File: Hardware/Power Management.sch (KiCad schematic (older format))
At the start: 15 parts

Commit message: Motor driver and power management subsheet converted to blocks
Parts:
- removed TP?: Bat+, TestPoint:TestPoint_Keystone_5000-5004_Miniature, symbol Connector:TestPoint
- removed TP?: Bat-, TestPoint:TestPoint_Keystone_5000-5004_Miniature, symbol Connector:TestPoint
- removed TP?: TestPoint_2Pole, TestPoint:TestPoint_2Pads_Pitch2.54mm_Drill0.8mm, symbol Connector:TestPoint_2Pole
- added C?: 220nF, Capacitor_Tantalum_SMD:CP_EIA-3216-18_Kemet-A, symbol Device:CP_Small
- added C? (x2): 4.7uF, Capacitor_Tantalum_SMD:CP_EIA-3528-15_AVX-H, symbol Device:CP_Small
- added C?: 100nF, Capacitor_SMD:C_0805_2012Metric, symbol Device:C_Small
- added C?: 100uF, Capacitor_Tantalum_SMD:CP_EIA-7343-31_Kemet-D, symbol Device:CP_Small
- added D?: GREEN, symbol Device:LED_Small
- added D?: 5A, Diode_SMD:D_SOD-123F, symbol Device:D_Schottky
- added L?: 15uH, Inductor_SMD:L_Neosid_SMs42, symbol Device:L_Small
- added R?: 10K, Resistor_SMD:R_0805_2012Metric, symbol Device:R_Small_US
- added R?: 5.8k, Resistor_SMD:R_0805_2012Metric, symbol Device:R_Small_US
- added R?: 4.7k, Resistor_SMD:R_0805_2012Metric, symbol Device:R_Small_US
- added U?: TPS56628, Package_SO:HSOP-8-1EP_3.9x4.9mm_P1.27mm_EP2.41x3.1mm_ThermalVias, symbol Power_Management:TPS56628
- gave numbers to parts that had none: 12
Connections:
- net labels added: 3.3V, 9V, SNS3, SNS9, VBAT
- net labels removed: +3.3V, VSNS3
- wire segments 44 -> 86
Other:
- moved on the sheet: C4, C5, C6, C7, C8, D1, D2, L1, R5, R6, R7

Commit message: Readme updated
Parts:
- gave numbers to parts that had none: 12
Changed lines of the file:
@@
 P 4150 3350
 AR Path="/5FF19FDD" Ref="#PWR?"  Part="1"
-AR Path="/5FF0069C/5FF19FDD" Ref="#PWR012"  Part="1"
-F 0 "#PWR012" H 4150 3200 50  0001 C CNN
+AR Path="/5FF0069C/5FF19FDD" Ref="#PWR015"  Part="1"
+F 0 "#PWR015" H 4150 3200 50  0001 C CNN
 F 1 "+BATT" H 4165 3523 50  0000 C CNN
 F 2 "" H 4150 3350 50  0001 C CNN
@@
 P 5600 3950
 AR Path="/5FF1A004" Ref="#PWR?"  Part="1"
-AR Path="/5FF0069C/5FF1A004" Ref="#PWR014"  Part="1"
-F 0 "#PWR014" H 5600 3700 50  0001 C CNN
+AR Path="/5FF0069C/5FF1A004" Ref="#PWR016"  Part="1"
+F 0 "#PWR016" H 5600 3700 50  0001 C CNN
 F 1 "GND" H 5605 3777 50  0000 C CNN
 F 2 "" H 5600 3950 50  0001 C CNN
@@
 AR Path="/5E9DAA7B/5FF43866" Ref="C?"  Part="1"
 AR Path="/5FF43866" Ref="C?"  Part="1"
-AR Path="/5FF0069C/5FF43866" Ref="C?"  Part="1"
-F 0 "C?" H 4638 5096 50  0000 L CNN
+AR Path="/5FF0069C/5FF43866" Ref="C11"  Part="1"
+F 0 "C11" H 4638 5096 50  0000 L CNN
 F 1 "220nF" H 4638 5005 50  0000 L CNN
 F 2 "Capacitor_Tantalum_SMD:CP_EIA-3216-18_Kemet-A" H 4550 5050 50  0001 C CNN
@@
 AR Path="/5E9DAA7B/5FF4386C" Ref="C?"  Part="1"
 AR Path="/5FF4386C" Ref="C?"  Part="1"
-AR Path="/5FF0069C/5FF4386C" Ref="C?"  Part="1"
-F 0 "C?" H 4238 5096 50  0000 L CNN
+AR Path="/5FF0069C/5FF4386C" Ref="C10"  Part="1"
+F 0 "C10" H 4238 5096 50  0000 L CNN
 F 1 "4.7uF" H 4238 5005 50  0000 L CNN
 F 2 "Capacitor_Tantalum_SMD:CP_EIA-3528-15_AVX-H" H 4150 5050 50  0001 C CNN
@@
 AR Path="/5E9DAA7B/5FF43873" Ref="L?"  Part="1"
 AR Path="/5FF43873" Ref="L?"  Part="1"
-AR Path="/5FF0069C/5FF43873" Ref="L?"  Part="1"
-F 0 "L?" V 6835 4800 50  0000 C CNN
+AR Path="/5FF0069C/5FF43873" Ref="L2"  Part="1"
+F 0 "L2" V 6835 4800 50  0000 C CNN
 F 1 "15uH" V 6744 4800 50  0000 C CNN
 F 2 "Inductor_SMD:L_Neosid_SMs42" H 6650 4800 50  0001 C CNN
@@
 AR Path="/5E9DAA7B/5FF43879" Ref="C?"  Part="1"
 AR Path="/5FF43879" Ref="C?"  Part="1"
-AR Path="/5FF0069C/5FF43879" Ref="C?"  Part="1"
-F 0 "C?" V 5971 4800 50  0000 C CNN
+AR Path="/5FF0069C/5FF43879" Ref="C9"  Part="1"
+F 0 "C9" V 5971 4800 50  0000 C CNN
 F 1 "100nF" V 6062 4800 50  0000 C CNN
 F 2 "Capacitor_SMD:C_0805_2012Metric" H 6200 4800 50  0001 C CNN
@@
 P 4150 4750
 AR Path="/5FF43888" Ref="#PWR?"  Part="1"
-AR Path="/5FF0069C/5FF43888" Ref="#PWR?"  Part="1"
-F 0 "#PWR?" H 4150 4600 50  0001 C CNN
+AR Path="/5FF0069C/5FF43888" Ref="#PWR017"  Part="1"
+F 0 "#PWR017" H 4150 4600 50  0001 C CNN
 F 1 "+BATT" H 4165 4923 50  0000 C CNN
 F 2 "" H 4150 4750 50  0001 C CNN
@@
 AR Path="/5E9DAA7B/5FF43896" Ref="R?"  Part="1"
 AR Path="/5FF43896" Ref="R?"  Part="1"
-AR Path="/5FF0069C/5FF43896" Ref="R?"  Part="1"
-F 0 "R?" H 7718 4900 50  0000 L BNN
+AR Path="/5FF0069C/5FF43896" Ref="R8"  Part="1"
+F 0 "R8" H 7718 4900 50  0000 L BNN
 F 1 "10K" H 7718 4855 50  0000 L CNN
 F 2 "Resistor_SMD:R_0805_2012Metric" H 7650 4900 50  0001 C CNN
@@
 AR Path="/5E9DAA7B/5FF4389C" Ref="R?"  Part="1"
 AR Path="/5FF4389C" Ref="R?"  Part="1"
-AR Path="/5FF0069C/5FF4389C" Ref="R?"  Part="1"
-F 0 "R?" H 7718 5200 50  0000 L BNN
+AR Path="/5FF0069C/5FF4389C" Ref="R10"  Part="1"
+F 0 "R10" H 7718 5200 50  0000 L BNN
 F 1 "5.8k" H 7718 5155 50  0000 L CNN
 F 2 "Resistor_SMD:R_0805_2012Metric" H 7650 5200 50  0001 C CNN
@@
 P 5600 5350
 AR Path="/5FF438A6" Ref="#PWR?"  Part="1"
-AR Path="/5FF0069C/5FF438A6" Ref="#PWR?"  Part="1"
-F 0 "#PWR?" H 5600 5100 50  0001 C CNN
+AR Path="/5FF0069C/5FF438A6" Ref="#PWR018"  Part="1"
+F 0 "#PWR018" H 5600 5100 50  0001 C CNN
 F 1 "GND" H 5605 5177 50  0000 C CNN
 F 2 "" H 5600 5350 50  0001 C CNN
@@
 P 4550 4750
 AR Path="/5FF438AD" Ref="#FLG?"  Part="1"
-AR Path="/5FF0069C/5FF438AD" Ref="#FLG?"  Part="1"
-F 0 "#FLG?" H 4550 4825 50  0001 C CNN
+AR Path="/5FF0069C/5FF438AD" Ref="#FLG04"  Part="1"
+F 0 "#FLG04" H 4550 4825 50  0001 C CNN
 F 1 "PWR_FLAG" H 4550 4923 50  0000 C CNN
 F 2 "" H 4550 4750 50  0001 C CNN
@@
 P 4550 5350
 AR Path="/5FF438B4" Ref="#FLG?"  Part="1"
-AR Path="/5FF0069C/5FF438B4" Ref="#FLG?"  Part="1"
-F 0 "#FLG?" H 4550 5425 50  0001 C CNN
+AR Path="/5FF0069C/5FF438B4" Ref="#FLG06"  Part="1"
+F 0 "#FLG06" H 4550 5425 50  0001 C CNN
 F 1 "PWR_FLAG" H 4550 5523 50  0000 C CNN
 F 2 "" H 4550 5350 50  0001 C CNN
@@
 P 7250 4750
 AR Path="/5FF438BB" Ref="#FLG?"  Part="1"
-AR Path="/5FF0069C/5FF438BB" Ref="#FLG?"  Part="1"
-F 0 "#FLG?" H 7250 4825 50  0001 C CNN
+AR Path="/5FF0069C/5FF438BB" Ref="#FLG05"  Part="1"
+F 0 "#FLG05" H 7250 4825 50  0001 C CNN
 F 1 "PWR_FLAG" H 7250 4923 50  0000 C CNN
 F 2 "" H 7250 4750 50  0001 C CNN
@@
 P 5600 4700
 AR Path="/5FF438C6" Ref="U?"  Part="1"
-AR Path="/5FF0069C/5FF438C6" Ref="U?"  Part="1"
-F 0 "U?" H 5600 4865 50  0000 C CNN
+AR Path="/5FF0069C/5FF438C6" Ref="U3"  Part="1"
+F 0 "U3" H 5600 4865 50  0000 C CNN
 F 1 "TPS56628" H 5600 4774 50  0000 C CNN
 F 2 "Package_SO:HSOP-8-1EP_3.9x4.9mm_P1.27mm_EP2.41x3.1mm_ThermalVias" H 5600 4850 50  0001 C CNN
@@
 P 5050 5100
 AR Path="/5FF438CF" Ref="D?"  Part="1"
-AR Path="/5FF0069C/5FF438CF" Ref="D?"  Part="1"
-F 0 "D?" H 4950 5200 50  0000 C CNN
+AR Path="/5FF0069C/5FF438CF" Ref="D4"  Part="1"
+F 0 "D4" H 4950 5200 50  0000 C CNN
 F 1 "GREEN" H 5150 5200 50  0000 C CNN
 F 2 "" V 5050 5100 50  0001 C CNN
@@
 AR Path="/5EA2026E/5FF438D5" Ref="R?"  Part="1"
 AR Path="/5FF438D5" Ref="R?"  Part="1"
-AR Path="/5FF0069C/5FF438D5" Ref="R?"  Part="1"
-F 0 "R?" V 5150 5050 50  0000 L CNN
+AR Path="/5FF0069C/5FF438D5" Ref="R9"  Part="1"
+F 0 "R9" V 5150 5050 50  0000 L CNN
 F 1 "4.7k" V 5100 4900 50  0000 L CNN
 F 2 "Resistor_SMD:R_0805_2012Metric" H 5050 5000 50  0001 C CNN
@@
 AR Path="/5E9DAA7B/5FF438EB" Ref="C?"  Part="1"
 AR Path="/5FF438EB" Ref="C?"  Part="1"
-AR Path="/5FF0069C/5FF438EB" Ref="C?"  Part="1"
-F 0 "C?" H 6938 5096 50  0000 L CNN
+AR Path="/5FF0069C/5FF438EB" Ref="C12"  Part="1"
+F 0 "C12" H 6938 5096 50  0000 L CNN
 F 1 "100uF" H 6938 5005 50  0000 L CNN
 F 2 "Capacitor_Tantalum_SMD:CP_EIA-7343-31_Kemet-D" H 6850 5050 50  0001 C CNN
@@
 AR Path="/5E9DAA7B/5FF438F1" Ref="C?"  Part="1"
 AR Path="/5FF438F1" Ref="C?"  Part="1"
-AR Path="/5FF0069C/5FF438F1" Ref="C?"  Part="1"
-F 0 "C?" H 7338 5096 50  0000 L CNN
+AR Path="/5FF0069C/5FF438F1" Ref="C13"  Part="1"
+F 0 "C13" H 7338 5096 50  0000 L CNN
 F 1 "4.7uF" H 7338 5005 50  0000 L CNN
 F 2 "Capacitor_Tantalum_SMD:CP_EIA-3528-15_AVX-H" H 7250 5050 50  0001 C CNN
@@
 AR Path="/5E9DAA7B/5FF438F7" Ref="D?"  Part="1"
 AR Path="/5FF438F7" Ref="D?"  Part="1"
-AR Path="/5FF0069C/5FF438F7" Ref="D?"  Part="1"
-F 0 "D?" V 6404 5129 50  0000 L CNN
+AR Path="/5FF0069C/5FF438F7" Ref="D3"  Part="1"
+F 0 "D3" V 6404 5129 50  0000 L CNN
 F 1 "5A" V 6495 5129 50  0000 L CNN
 F 2 "Diode_SMD:D_SOD-123F" V 6450 5050 50  0001 C CNN

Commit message: Tidying up
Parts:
- U2, U3: symbol Power_Management:TPS56628 -> tps56628:TPS56628
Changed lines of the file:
@@
 Tant
 $Comp
-L Power_Management:TPS56628 U?
+L tps56628:TPS56628 U?
 U 1 1 5FF1A031
 P 5600 3300
@@
 Tant
 $Comp
-L Power_Management:TPS56628 U?
+L tps56628:TPS56628 U?
 U 1 1 5FF438C6
 P 5600 4700

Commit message: Battery charger IC added
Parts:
- added TP? (x2): TestPoint, TestPoint:TestPoint_Loop_D1.80mm_Drill1.0mm_Beaded, symbol Connector:TestPoint
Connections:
- net 3.3V: now also TP?.1
- net 9V: now also TP?.1
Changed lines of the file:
@@
 Wire Wire Line
 	4150 4800 4100 4800
+$Comp
+L Connector:TestPoint TP?
+U 1 1 5FF08244
+P 7650 3350
+F 0 "TP?" H 7708 3422 50  0000 L CNN
+F 1 "TestPoint" H 7708 3377 50  0001 L CNN
+F 2 "TestPoint:TestPoint_Loop_D1.80mm_Drill1.0mm_Beaded" H 7850 3350 50  0001 C CNN
+F 3 "~" H 7850 3350 50  0001 C CNN
+	1    7650 3350
+	1    0    0    -1
+$EndComp
+Wire Wire Line
+	7650 3350 7650 3400
+$Comp
+L Connector:TestPoint TP?
+U 1 1 5FF0F95D
+P 7650 4750
+F 0 "TP?" H 7708 4822 50  0000 L CNN
+F 1 "TestPoint" H 7708 4777 50  0001 L CNN
+F 2 "TestPoint:TestPoint_Loop_D1.80mm_Drill1.0mm_Beaded" H 7850 4750 50  0001 C CNN
+F 3 "~" H 7850 4750 50  0001 C CNN
+	1    7650 4750
+	1    0    0    -1
+$EndComp
+Wire Wire Line
+	7650 4750 7650 4800
 $EndSCHEMATC

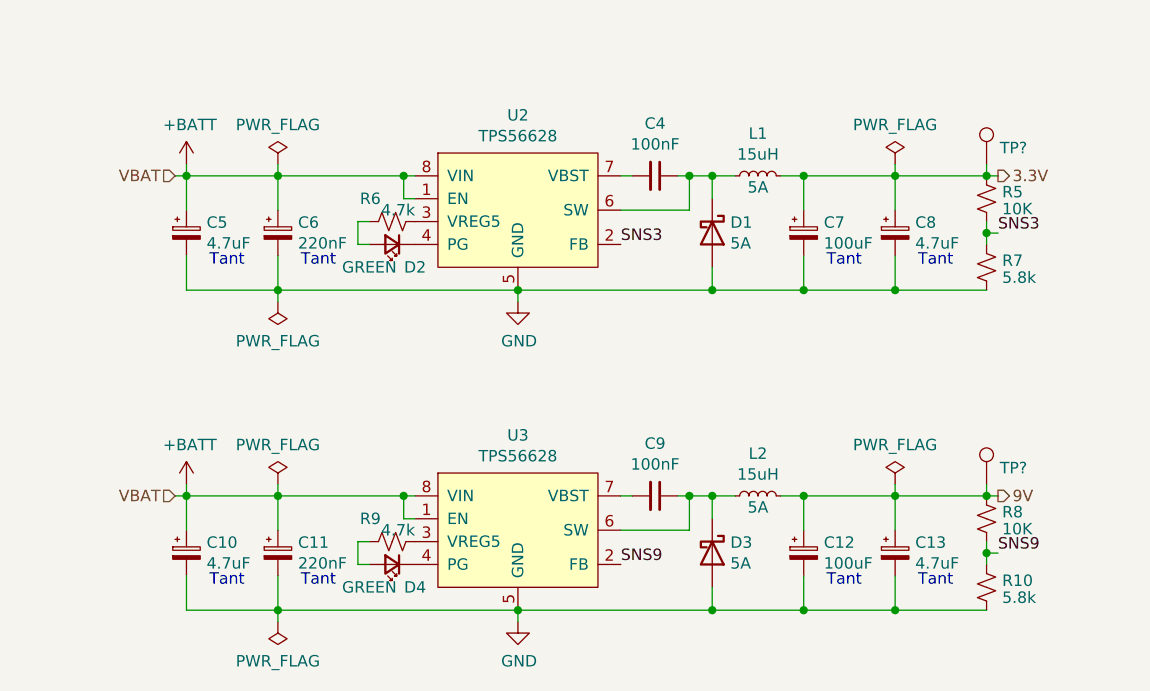
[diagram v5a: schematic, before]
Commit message: Replaced ESP-WROOM-32D with ESP32-CAM
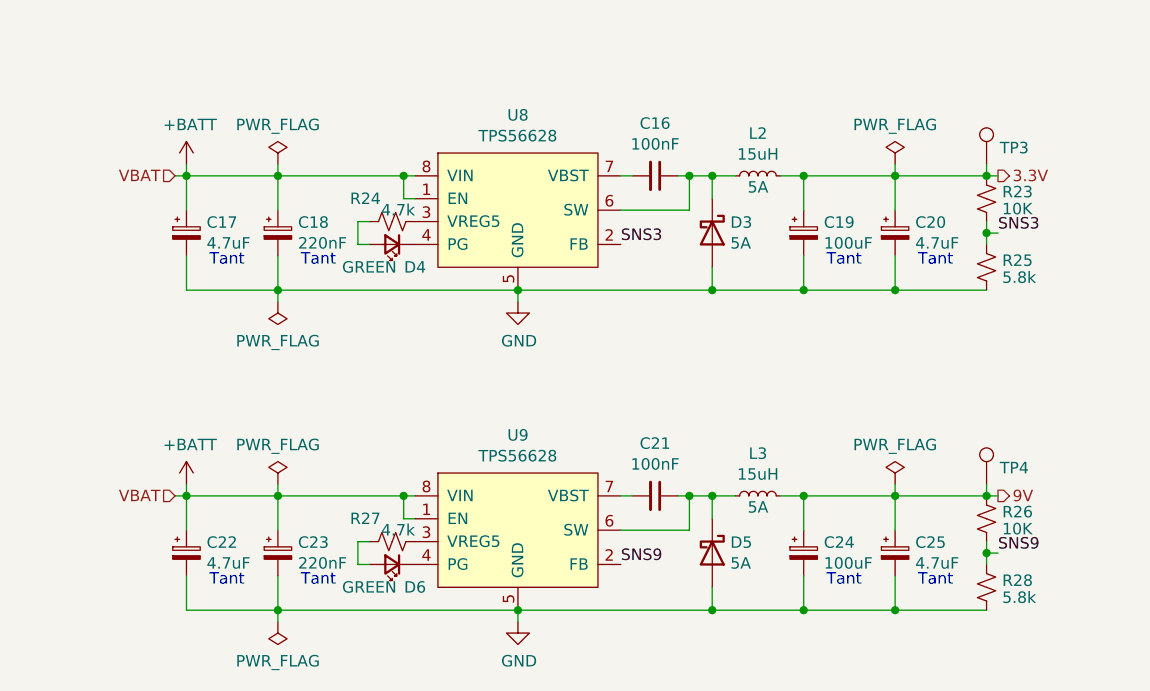
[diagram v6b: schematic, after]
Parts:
- gave numbers to parts that had none: 2
- renumbered C4 to C16, C5 to C17, C6 to C18, C7 to C19, C8 to C20, C9 to C21, C10 to C22, C11 to C23, C12 to C24, C13 to C25, D1 to D3, D2 to D4, D3 to D5, D4 to D6, L1 to L2, L2 to L3, R5 to R23, R6 to R24, R7 to R25, R8 to R26, R9 to R27, R10 to R28, U2 to U8, U3 to U9

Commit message: Signed-off-by: Usman <usmanmehmood55@gmail.com>
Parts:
- renumbered R23 to R25, R24 to R26, R25 to R27, R26 to R28, R27 to R29, R28 to R30
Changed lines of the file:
@@
 AR Path="/5E9DAA7B/5FF19FF3" Ref="R?"  Part="1"
 AR Path="/5FF19FF3" Ref="R?"  Part="1"
-AR Path="/5FF0069C/5FF19FF3" Ref="R23"  Part="1"
-F 0 "R23" H 7718 3500 50  0000 L BNN
+AR Path="/5FF0069C/5FF19FF3" Ref="R25"  Part="1"
+F 0 "R25" H 7718 3500 50  0000 L BNN
 F 1 "10K" H 7718 3455 50  0000 L CNN
 F 2 "Resistor_SMD:R_0805_2012Metric" H 7650 3500 50  0001 C CNN
@@
 AR Path="/5E9DAA7B/5FF19FF9" Ref="R?"  Part="1"
 AR Path="/5FF19FF9" Ref="R?"  Part="1"
-AR Path="/5FF0069C/5FF19FF9" Ref="R25"  Part="1"
-F 0 "R25" H 7718 3800 50  0000 L BNN
+AR Path="/5FF0069C/5FF19FF9" Ref="R27"  Part="1"
+F 0 "R27" H 7718 3800 50  0000 L BNN
 F 1 "5.8k" H 7718 3755 50  0000 L CNN
 F 2 "Resistor_SMD:R_0805_2012Metric" H 7650 3800 50  0001 C CNN
@@
 Wire Wire Line
 	5600 3950 5600 3900
-$Comp
-L power:PWR_FLAG #FLG?
-U 1 1 5FF1A018
-P 4550 3350
-AR Path="/5FF1A018" Ref="#FLG?"  Part="1"
-AR Path="/5FF0069C/5FF1A018" Ref="#FLG01"  Part="1"
-F 0 "#FLG01" H 4550 3425 50  0001 C CNN
-F 1 "PWR_FLAG" H 4550 3523 50  0000 C CNN
-F 2 "" H 4550 3350 50  0001 C CNN
-F 3 "~" H 4550 3350 50  0001 C CNN
-	1    4550 3350
-	1    0    0    -1
-$EndComp
-Wire Wire Line
-	4550 3350 4550 3400
-$Comp
-L power:PWR_FLAG #FLG?
-U 1 1 5FF1A01F
-P 4550 3950
-AR Path="/5FF1A01F" Ref="#FLG?"  Part="1"
-AR Path="/5FF0069C/5FF1A01F" Ref="#FLG03"  Part="1"
-F 0 "#FLG03" H 4550 4025 50  0001 C CNN
-F 1 "PWR_FLAG" H 4550 4123 50  0000 C CNN
-F 2 "" H 4550 3950 50  0001 C CNN
-F 3 "~" H 4550 3950 50  0001 C CNN
-	1    4550 3950
-	-1   0    0    1
-$EndComp
-Wire Wire Line
-	4550 3950 4550 3900
-$Comp
-L power:PWR_FLAG #FLG?
-U 1 1 5FF1A026
-P 7250 3350
-AR Path="/5FF1A026" Ref="#FLG?"  Part="1"
-AR Path="/5FF0069C/5FF1A026" Ref="#FLG02"  Part="1"
-F 0 "#FLG02" H 7250 3425 50  0001 C CNN
-F 1 "PWR_FLAG" H 7250 3523 50  0000 C CNN
-F 2 "" H 7250 3350 50  0001 C CNN
-F 3 "~" H 7250 3350 50  0001 C CNN
-	1    7250 3350
-	1    0    0    -1
-$EndComp
-Wire Wire Line
-	7250 3350 7250 3400
 Text Notes 6950 3800 0    50   ~ 0
 Tant
@@
 AR Path="/5EA2026E/5FF1A040" Ref="R?"  Part="1"
 AR Path="/5FF1A040" Ref="R?"  Part="1"
-AR Path="/5FF0069C/5FF1A040" Ref="R24"  Part="1"
-F 0 "R24" V 5150 3650 50  0000 L CNN
+AR Path="/5FF0069C/5FF1A040" Ref="R26"  Part="1"
+F 0 "R26" V 5150 3650 50  0000 L CNN
 F 1 "4.7k" V 5100 3500 50  0000 L CNN
 F 2 "Resistor_SMD:R_0805_2012Metric" H 5050 3600 50  0001 C CNN
@@
 AR Path="/5E9DAA7B/5FF43896" Ref="R?"  Part="1"
 AR Path="/5FF43896" Ref="R?"  Part="1"
-AR Path="/5FF0069C/5FF43896" Ref="R26"  Part="1"
-F 0 "R26" H 7718 4900 50  0000 L BNN
+AR Path="/5FF0069C/5FF43896" Ref="R28"  Part="1"
+F 0 "R28" H 7718 4900 50  0000 L BNN
 F 1 "10K" H 7718 4855 50  0000 L CNN
 F 2 "Resistor_SMD:R_0805_2012Metric" H 7650 4900 50  0001 C CNN
@@
 AR Path="/5E9DAA7B/5FF4389C" Ref="R?"  Part="1"
 AR Path="/5FF4389C" Ref="R?"  Part="1"
-AR Path="/5FF0069C/5FF4389C" Ref="R28"  Part="1"
-F 0 "R28" H 7718 5200 50  0000 L BNN
+AR Path="/5FF0069C/5FF4389C" Ref="R30"  Part="1"
+F 0 "R30" H 7718 5200 50  0000 L BNN
 F 1 "5.8k" H 7718 5155 50  0000 L CNN
 F 2 "Resistor_SMD:R_0805_2012Metric" H 7650 5200 50  0001 C CNN
@@
 Wire Wire Line
 	5600 5350 5600 5300
-$Comp
-L power:PWR_FLAG #FLG?
-U 1 1 5FF438AD
-P 4550 4750
-AR Path="/5FF438AD" Ref="#FLG?"  Part="1"
-AR Path="/5FF0069C/5FF438AD" Ref="#FLG04"  Part="1"
-F 0 "#FLG04" H 4550 4825 50  0001 C CNN
-F 1 "PWR_FLAG" H 4550 4923 50  0000 C CNN
-F 2 "" H 4550 4750 50  0001 C CNN
-F 3 "~" H 4550 4750 50  0001 C CNN
-	1    4550 4750
-	1    0    0    -1
-$EndComp
-Wire Wire Line
-	4550 4750 4550 4800
-$Comp
-L power:PWR_FLAG #FLG?
-U 1 1 5FF438B4
-P 4550 5350
-AR Path="/5FF438B4" Ref="#FLG?"  Part="1"
-AR Path="/5FF0069C/5FF438B4" Ref="#FLG06"  Part="1"
-F 0 "#FLG06" H 4550 5425 50  0001 C CNN
-F 1 "PWR_FLAG" H 4550 5523 50  0000 C CNN
-F 2 "" H 4550 5350 50  0001 C CNN
-F 3 "~" H 4550 5350 50  0001 C CNN
-	1    4550 5350
-	-1   0    0    1
-$EndComp
-Wire Wire Line
-	4550 5350 4550 5300
-$Comp
-L power:PWR_FLAG #FLG?
-U 1 1 5FF438BB
-P 7250 4750
-AR Path="/5FF438BB" Ref="#FLG?"  Part="1"
-AR Path="/5FF0069C/5FF438BB" Ref="#FLG05"  Part="1"
-F 0 "#FLG05" H 7250 4825 50  0001 C CNN
-F 1 "PWR_FLAG" H 7250 4923 50  0000 C CNN
-F 2 "" H 7250 4750 50  0001 C CNN
-F 3 "~" H 7250 4750 50  0001 C CNN
-	1    7250 4750
-	1    0    0    -1
-$EndComp
-Wire Wire Line
-	7250 4750 7250 4800
 Text Notes 6950 5200 0    50   ~ 0
 Tant
@@
 AR Path="/5EA2026E/5FF438D5" Ref="R?"  Part="1"
 AR Path="/5FF438D5" Ref="R?"  Part="1"
-AR Path="/5FF0069C/5FF438D5" Ref="R27"  Part="1"
-F 0 "R27" V 5150 5050 50  0000 L CNN
+AR Path="/5FF0069C/5FF438D5" Ref="R29"  Part="1"
+F 0 "R29" V 5150 5050 50  0000 L CNN
 F 1 "4.7k" V 5100 4900 50  0000 L CNN
 F 2 "Resistor_SMD:R_0805_2012Metric" H 5050 5000 50  0001 C CNN
@@
 Wire Wire Line
 	7650 4750 7650 4800
+Wire Wire Line
+	7250 4750 7250 4800
+$Comp
+L power:PWR_FLAG #FLG?
+U 1 1 5FF438BB
+P 7250 4750
+AR Path="/5FF438BB" Ref="#FLG?"  Part="1"
+AR Path="/5FF0069C/5FF438BB" Ref="#FLG05"  Part="1"
+F 0 "#FLG05" H 7250 4825 50  0001 C CNN
+F 1 "PWR_FLAG" H 7250 4923 50  0000 C CNN
+F 2 "" H 7250 4750 50  0001 C CNN
+F 3 "~" H 7250 4750 50  0001 C CNN
+	1    7250 4750
+	1    0    0    -1
+$EndComp
+Wire Wire Line
+	7250 3350 7250 3400
+$Comp
+L power:PWR_FLAG #FLG?
+U 1 1 6071CB78
+P 7250 3350
+AR Path="/6071CB78" Ref="#FLG?"  Part="1"
+AR Path="/5FF0069C/6071CB78" Ref="#FLG0103"  Part="1"
+F 0 "#FLG0103" H 7250 3425 50  0001 C CNN
+F 1 "PWR_FLAG" H 7250 3523 50  0000 C CNN
+F 2 "" H 7250 3350 50  0001 C CNN
+F 3 "~" H 7250 3350 50  0001 C CNN
+	1    7250 3350
+	1    0    0    -1
+$EndComp
 $EndSCHEMATC
